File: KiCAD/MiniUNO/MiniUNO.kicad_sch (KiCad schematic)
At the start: 19 parts, among them J1 USB_B_Micro, J2 Conn_01x11, J3 Conn_01x11, J4 Conn_01x07, U1 ATmega32U4-A, Y1 830108288709

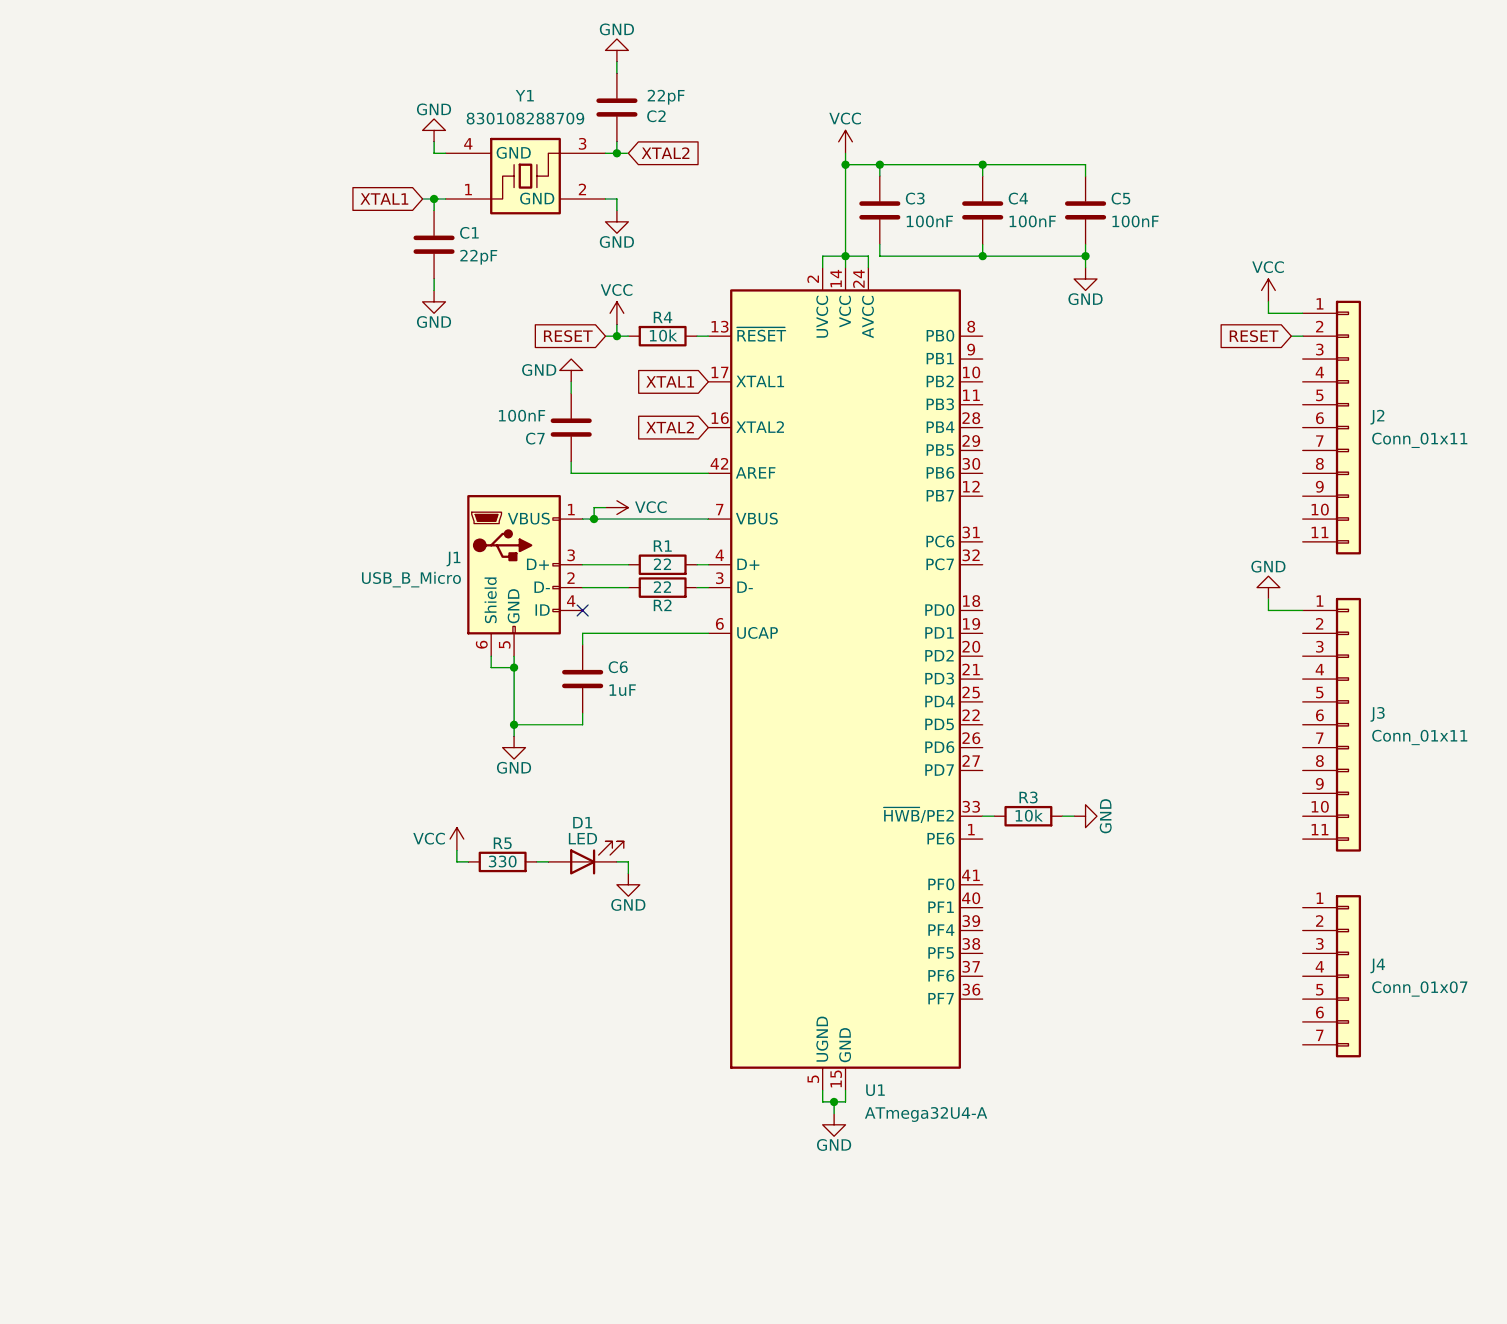
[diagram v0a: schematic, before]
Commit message: Added a user controlled LED
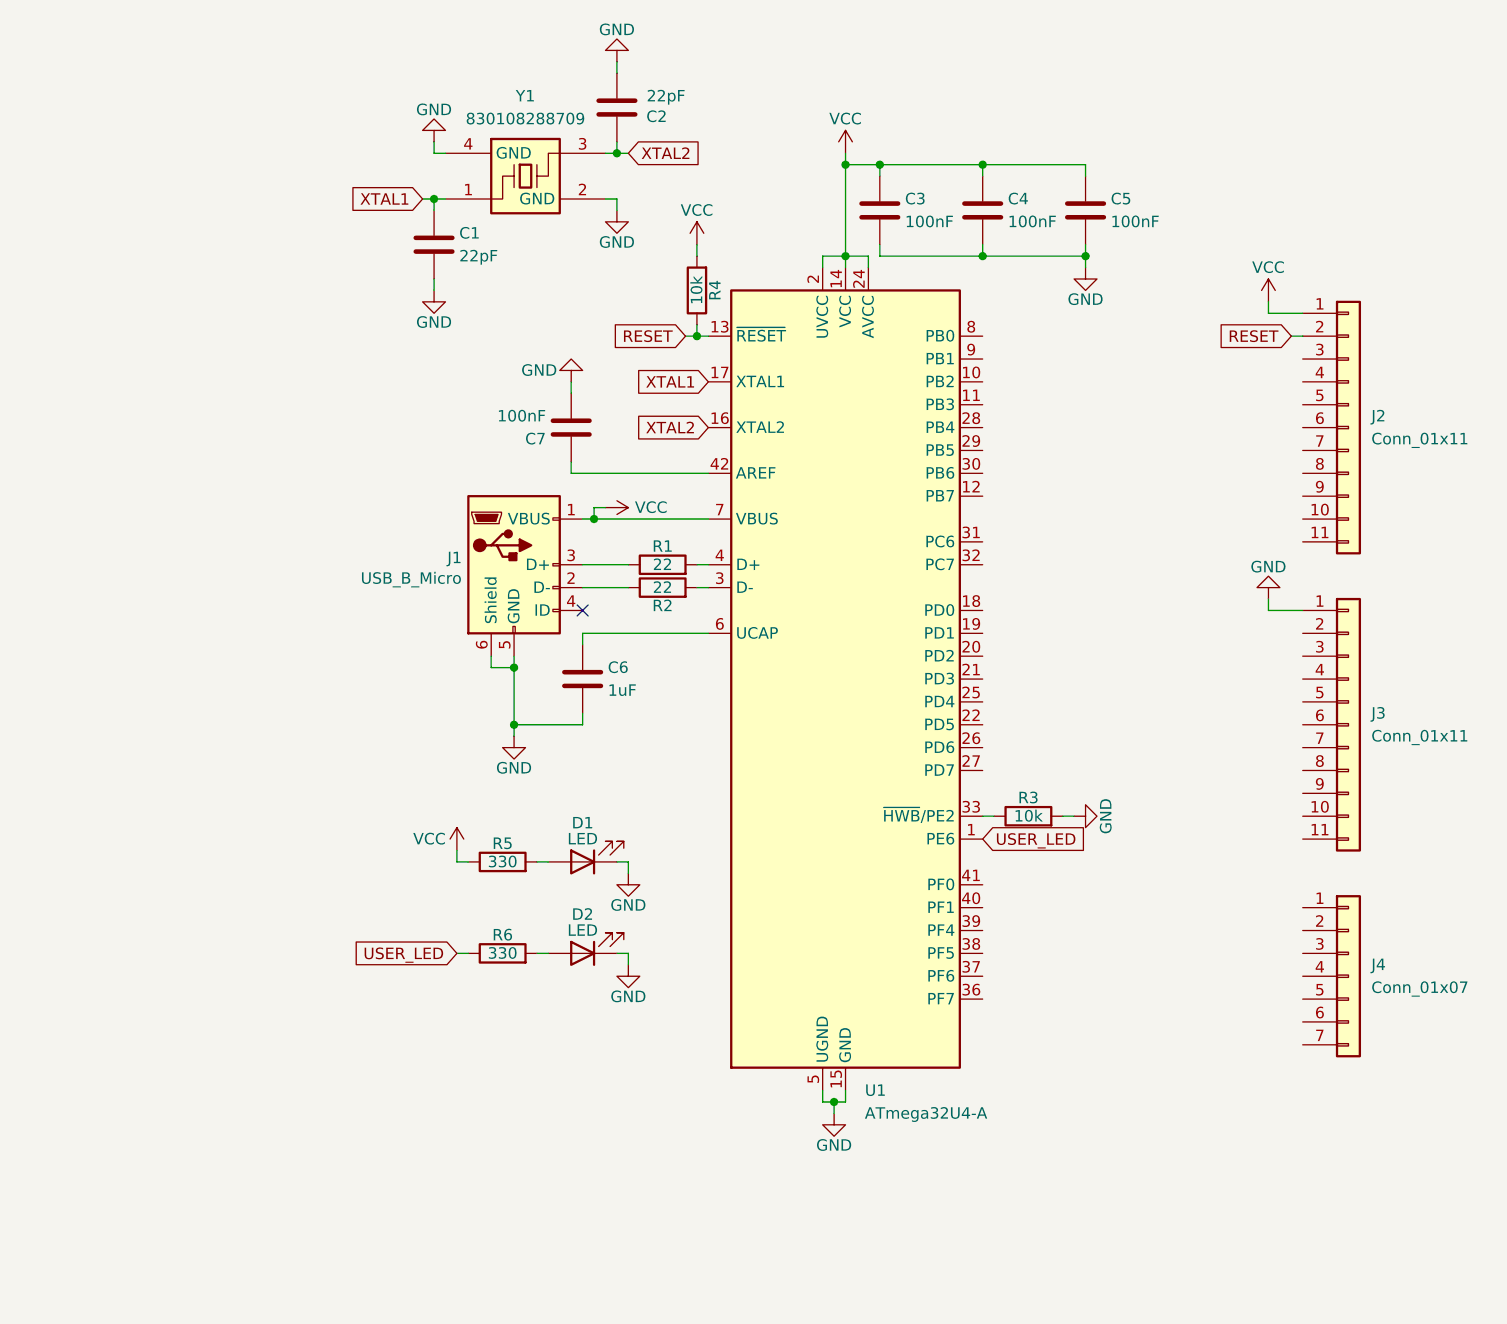
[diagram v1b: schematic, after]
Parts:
- added D2: LED, LED_SMD:LED_0603_1608Metric, symbol Device:LED
- added R6: 330, Resistor_SMD:R_0603_1608Metric, symbol Device:R
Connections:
- net GND: now also D2.1 (K)
- net VCC: no longer J2.2 (Pin_2)
- net RESET: now reaches R4.1, U1.13 (~{RESET})
- net RESET: now also J2.2 (Pin_2)
- net USER_LED: now reaches U1.1 (PE6)
- net USER_LED: now also R6.1
- new net: D2.2 (A), R6.2
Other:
- moved on the sheet: R4

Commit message: Minor changes
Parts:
- Y1: footprint Crystal:830108288709 -> Crystal:830108288709_Handsolderable
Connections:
- net MOSI: now reaches U1.10 (PB2)
- net MOSI: now also J2.5 (Pin_5)
- net MISO: now reaches U1.11 (PB3)
- net MISO: now also J2.6 (Pin_6)
- net D11: now reaches U1.12 (PB7)
- net D11: now also J3.11 (Pin_11)
- net D3/SCL: now reaches U1.18 (PD0)
- net D3/SCL: now also J2.11 (Pin_11)
- net D2/SDA: now reaches U1.19 (PD1)
- net D2/SDA: now also J2.10 (Pin_10)
- net D0/RX: now reaches U1.20 (PD2)
- net D0/RX: now also J2.8 (Pin_8)
- net D1/TX: now reaches U1.21 (PD3)
- net D1/TX: now also J2.9 (Pin_9)
- net CTS: now reaches U1.22 (PD5)
- net CTS: now also J2.7 (Pin_7)
- net D4: now reaches U1.25 (PD4)
- net D4: now also J4.1 (Pin_1)
- net D12: now reaches U1.26 (PD6)
- net D12: now also J3.10 (Pin_10)
- net D6: now reaches U1.27 (PD7)
- net D6: now also J4.3 (Pin_3)
- net D8: now reaches U1.28 (PB4)
- net D8: now also J4.5 (Pin_5)
- net D9: now reaches U1.29 (PB5)
- net D9: now also J4.6 (Pin_6)
- net D10: now reaches U1.30 (PB6)
- net D10: now also J4.7 (Pin_7)
- net D5: now reaches U1.31 (PC6)
- net D5: now also J4.2 (Pin_2)
- net D13/USER_LED: now reaches U1.32 (PC7)
- net D13/USER_LED: now also J3.9 (Pin_9), R6.1
- net A0: now reaches U1.36 (PF7)
- net A0: now also J3.8 (Pin_8)
- net A1: now reaches U1.37 (PF6)
- net A1: now also J3.7 (Pin_7)
- net A2: now reaches U1.38 (PF5)
- net A2: now also J3.6 (Pin_6)
- net A3: now reaches U1.39 (PF4)
- net A3: now also J3.5 (Pin_5)
- net A4: now reaches U1.40 (PF1)
- net A4: now also J3.4 (Pin_4)
- net A5: now reaches U1.41 (PF0)
- net A5: now also J3.3 (Pin_3)
- net AREF: now reaches C7.1, U1.42 (AREF)
- net AREF: now also J3.2 (Pin_2)
- net SS: now reaches U1.8 (PB0)
- net SS: now also J2.3 (Pin_3)
- net SCK: now reaches U1.9 (PB1)
- net SCK: now also J2.4 (Pin_4)
- net D7: now reaches J4.4 (Pin_4)
- net D7: now also U1.1 (PE6)
- removed net USER_LED: R6.1, U1.1 (PE6)

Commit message: Lots more work
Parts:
- added C8: 22uF, Capacitor_SMD:C_0603_1608Metric, symbol Device:C
- added C9: 10uF, Capacitor_SMD:C_0603_1608Metric, symbol Device:C
- added IC1: AZ1117CR2-5.0TRG1, AZ1117CR2-5.0TRG1:AP738133Y13, symbol AZ1117CR2-5_0TRG1:AZ1117CR2-5.0TRG1
- added Q1: FDN340P, Package_TO_SOT_SMD:SuperSOT-3, symbol Transistor_FET:FDN340P
- added Q2: PMV48XP, Package_TO_SOT_SMD:SOT-23, symbol Transistor_FET:FDN340P
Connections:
- net AREF: no longer J3.2 (Pin_2)
- net GND: now also C8.2, C9.2, IC1.1 (GND)
- net D-: now reaches R2.2, U1.3 (D-)
- net D+: now reaches R1.2, U1.4 (D+)
- net UCAP: now reaches C6.1, U1.6 (UCAP)
- net VCC renamed +5V
- net +5V: now also C8.1, IC1.3 (OUT), Q1.2 (S), Q2.1 (G); no longer J1.1 (VBUS), U1.7 (VBUS)
- new net: C9.1, IC1.2 (IN), Q2.2 (S)
- new net VIN: J3.2 (Pin_2), Q1.1 (G), Q2.3 (D)
- new net VUSB: J1.1 (VBUS), Q1.3 (D), U1.7 (VBUS)
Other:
- moved on the sheet: C1, C2, C6, D1, D2, J1, R1, R2, R5, R6, Y1

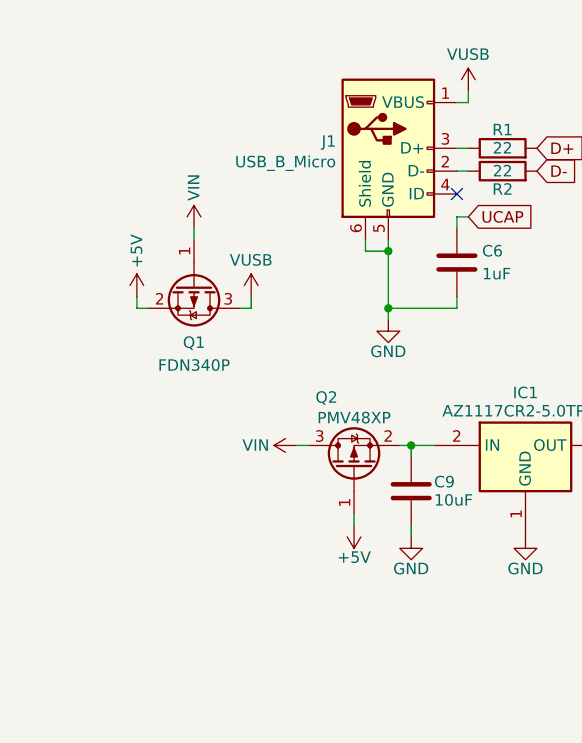
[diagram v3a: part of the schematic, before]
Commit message: Addec pulldown resistors to the VUSB and VIN MOSFETS. Made the adapter PCB
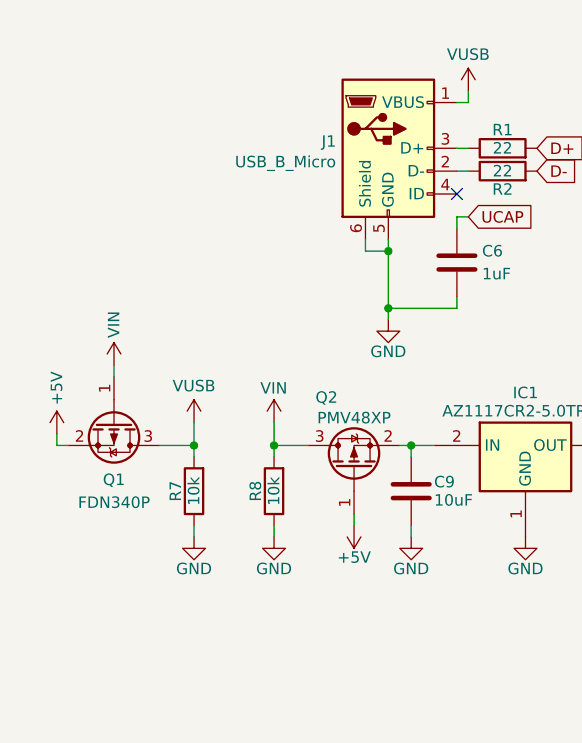
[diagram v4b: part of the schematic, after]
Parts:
- added R7, R8: 10k, Resistor_SMD:R_0603_1608Metric, symbol Device:R
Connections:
- net GND: now also R7.1, R8.1
- net VIN: now also R8.2
- net VUSB: now also R7.2
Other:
- moved on the sheet: Q1

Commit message: Finalized design v1
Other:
- moved on the sheet: C8, C9, IC1, Q1, Q2, R7, R8
